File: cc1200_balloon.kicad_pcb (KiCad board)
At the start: 4 copper layers, 50 x 30 mm, 117 parts, among them J101 BATT pads, J201 LoRa ANT pads, J202 SWD+DBG pads, J301 434MHz ANT pads, J401 GNSS ANT, J501 BMV080, Q101 DMG3401LSN-7, Q102 DMG3401LSN-7, SW101 PWR, U201 Wio-E5, U301 CC1200, U401 AT6558R-5N32, U501 SCD40-D-R2, U502 AS3935-BQFT, U503 BME688, U504 BME688, X301 40MHz, X401 TCXO 26MHz, X402 32.768kHz

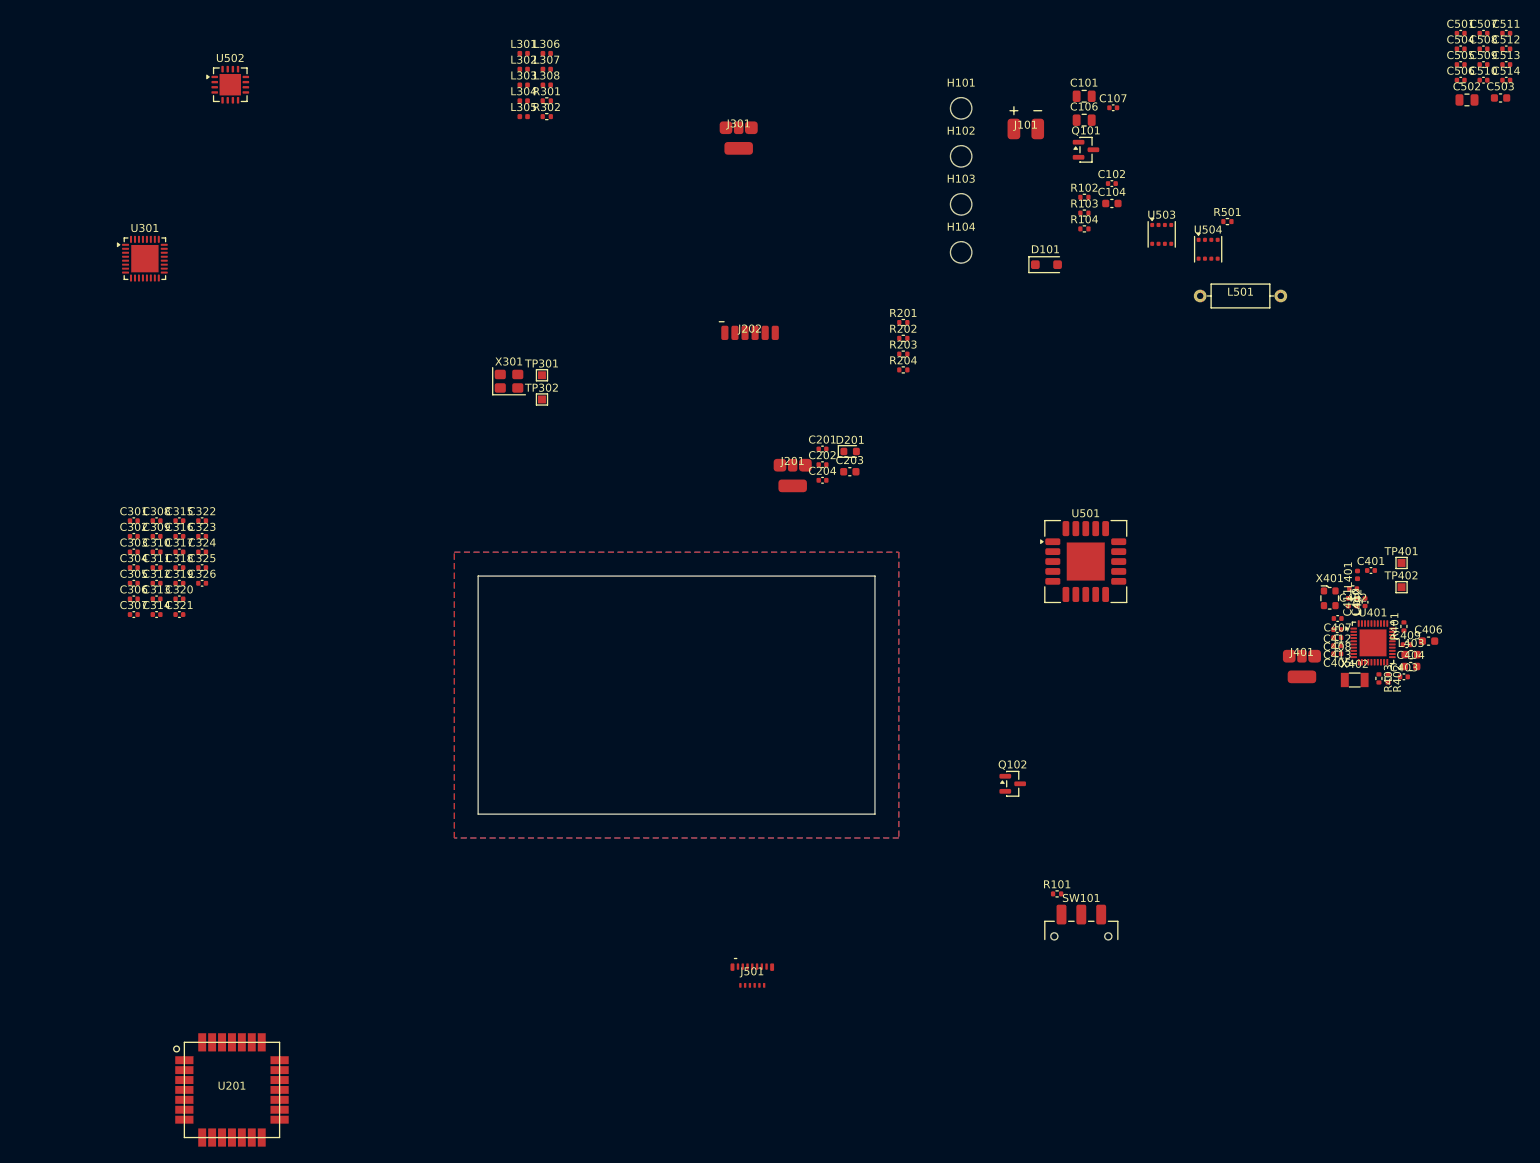
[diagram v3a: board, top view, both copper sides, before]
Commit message: Clean up schematic. Add component groups to PCB.
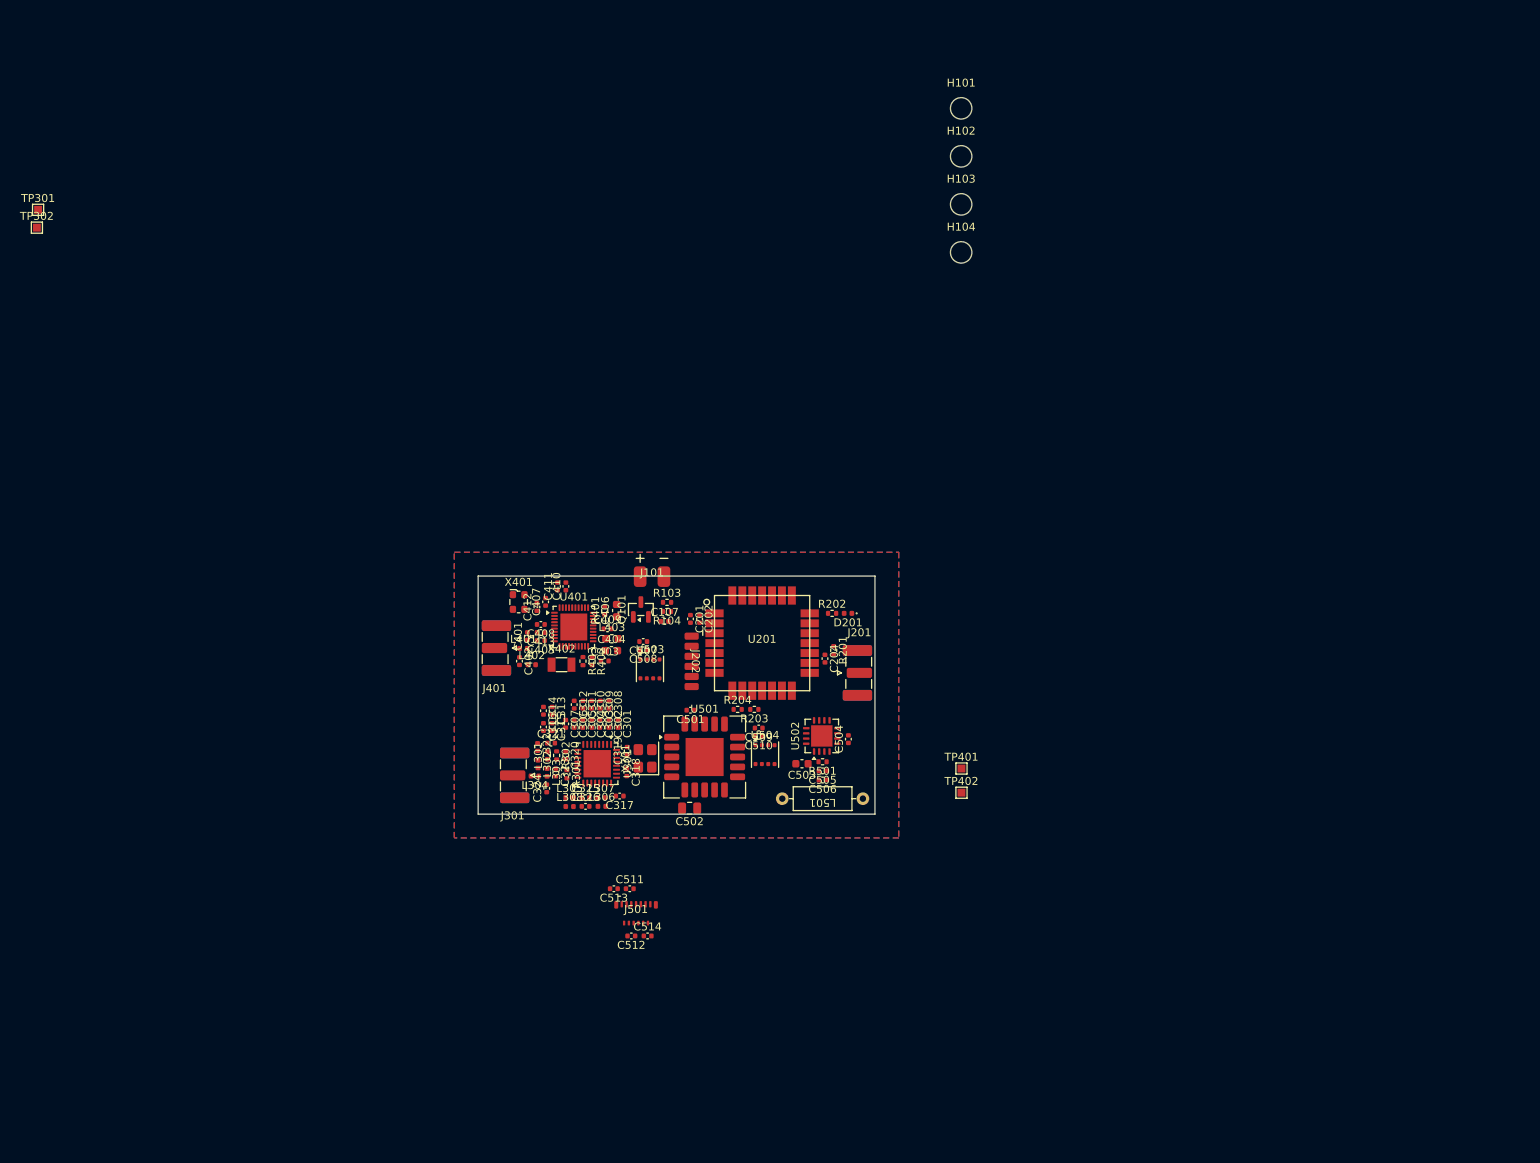
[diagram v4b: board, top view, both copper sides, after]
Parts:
- removed C101, C106: 22u, Capacitor_SMD:C_0805_2012Metric
- removed C102: 1u, Capacitor_SMD:C_0402_1005Metric
- removed C104, C203: 10u, Capacitor_SMD:C_0603_1608Metric
- removed D101: SMF6.5A, Diode_SMD:D_SOD-123F
- removed Q102: DMG3401LSN-7, Package_TO_SOT_SMD:SOT-23
- removed R101: 100k, Resistor_SMD:R_0402_1005Metric
- removed R102: 10k, Resistor_SMD:R_0402_1005Metric
- removed SW101: PWR, Button_Switch_SMD:SW_SPDT_CK_JS102011SAQN
- C202: value 1u -> 4.7u
- D201: footprint LED_SMD:LED_0603_1608Metric -> LED_SMD:LED_0402_1005Metric
- J201, J301, J401: footprint cc1200_balloon:SolderPad_Coax_Pigtail -> Connector_Coaxial:SMA_Samtec_SMA-J-P-H-ST-EM1_EdgeMount
- moved C512 157.0 mm to (94.3, 130.3), turned to 180 degrees
- moved C511 154.3 mm to (94.1, 124.4)
- moved C513 153.1 mm to (92.1, 124.4), turned to 180 degrees
- moved C514 152.8 mm to (96.3, 130.3)
- moved C502 132.5 mm to (101.7, 114.2), turned to 180 degrees
- moved C507 130.7 mm to (95.8, 93.2), turned to 180 degrees
- moved C508 130.2 mm to (95.8, 94.3), turned to 180 degrees
- moved C501 129.2 mm to (101.8, 101.9), turned to 180 degrees
- moved C509 123.8 mm to (110.3, 104.2), turned to 180 degrees
- moved C510 123.2 mm to (110.3, 105.2), turned to 180 degrees
- moved C503 121.6 mm to (115.8, 108.7), turned to 180 degrees
- moved C505 119.9 mm to (118.4, 109.5), turned to 180 degrees
- moved C506 119.3 mm to (118.4, 110.7), turned to 180 degrees
- moved C504 116.3 mm to (121.7, 105.5), turned to 90 degrees
- moved U502 110.9 mm to (118.3, 105.2), turned to 90 degrees
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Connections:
- net /Power/VBAT_IN renamed /MCU/VBATT_IN
- net VBAT_SENSE renamed /MCU/BATT_VSENSE
- C317 pad 1: Net-(U301-LPF0) -> Net-(U301-LPF1)
- C317 pad 2: Net-(U301-LPF1) -> Net-(U301-LPF0)
- C321 pad 1: /CC1200 Radio/RF_PA -> /CC1200 Radio/RF_TX1
- C321 pad 2: /CC1200 Radio/RF_TX1 -> /CC1200 Radio/RF_PA
- C325 pad 1: /CC1200 Radio/RF_LNAP -> /CC1200 Radio/RF_RX1
- C325 pad 2: /CC1200 Radio/RF_RX1 -> /CC1200 Radio/RF_LNAP
- C505 pad 1: Net-(C505-Pad1) -> /Sensors/AS_ANT_P
- L501 pad 1: Net-(C505-Pad1) -> /Sensors/AS_ANT_P
- Q101 pad 2: VBATT -> +BATT
- R501 pad 1: Net-(C505-Pad1) -> /Sensors/AS_ANT_P
- U501 pad 10: SDA -> SCL
- U501 pad 9: SCL -> SDA
- U502 pad 11: SCL -> SDA
- U502 pad 13: SDA -> SCL
- U503 pad 3: SDA -> SCL
- U503 pad 4: SCL -> SDA
- U504 pad 3: SDA -> SCL
- U504 pad 4: SCL -> SDA

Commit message: Inital routing
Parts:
- removed C502: 22u, Capacitor_SMD:C_0805_2012Metric
- removed C512, C513: 1u, Capacitor_SMD:C_0402_1005Metric
- removed C514: 100n, Capacitor_SMD:C_0402_1005Metric
- J101, J202: moved to B.Cu
- moved TP302 62.3 mm to (66.8, 81.5)
- moved TP301 62.2 mm to (66.8, 79.2)
- moved R104 48.7 mm to (50.1, 89.5)
- moved C107 48.7 mm to (49.8, 90.8)
- moved Q101 48.7 mm to (46.8, 89.3)
- moved R103 48.7 mm to (50.1, 88.4)
- moved J101 47.5 mm to (49.5, 87.7), turned to 180 degrees
- moved L501 33.5 mm to (97.1, 87.2), turned to 0 degrees
- moved C506 30.0 mm to (97.1, 89.5), turned to 0 degrees
- moved C504 29.5 mm to (94.1, 95.0), turned to -90 degrees
- moved C505 28.4 mm to (97.1, 90.7), turned to 0 degrees
- moved R501 27.0 mm to (97.1, 91.8), turned to 0 degrees
- moved C503 24.5 mm to (99.0, 90.8), turned to 90 degrees
- moved U502 23.4 mm to (97.2, 95.1), turned to -90 degrees
- moved C501 22.0 mm to (80.0, 99.1)
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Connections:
- U501 pad 10: SCL -> SDA
- U501 pad 9: SDA -> SCL
- U502 pad 11: SDA -> SCL
- U502 pad 13: SCL -> SDA
- U503 pad 3: SCL -> SDA
- U503 pad 4: SDA -> SCL
- U504 pad 3: SCL -> SDA
- U504 pad 4: SDA -> SCL
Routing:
- net +BATT: track 0.00 -> 21.0 mm, vias 0 -> 1
- net SPI_MISO: track 0.00 -> 18.1 mm, vias 0 -> 1
- net /CC1200 Radio/XOSC_Q1: track 0.00 -> 8.01 mm
- net /CC1200 Radio/RF_LNAN: track 0.00 -> 5.81 mm
- net /CC1200 Radio/RF_TX2: track 0.00 -> 4.57 mm
- net /CC1200 Radio/RF_PA: track 0.00 -> 4.37 mm
- net /CC1200 Radio/RF_TRXSW: track 0.00 -> 4.16 mm
- net /CC1200 Radio/RF_LNAP: track 0.00 -> 3.93 mm
- net /CC1200 Radio/XOSC_Q2: track 0.00 -> 3.80 mm
- net /CC1200 Radio/RF_RX1: track 0.00 -> 3.70 mm
- net SPI_MOSI: track 0.00 -> 3.55 mm, vias 0 -> 1
- net /CC1200 Radio/CC_RBIAS: track 0.00 -> 3.42 mm
- net Net-(U301-LPF1): track 0.00 -> 3.13 mm
- net Net-(U301-LPF0): track 0.00 -> 3.03 mm
- net RADIO_CS: track 0.00 -> 2.28 mm, vias 0 -> 1
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
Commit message: More routing.
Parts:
- TP301, TP302, TP401, TP402: moved to B.Cu
- moved R103 90.5 mm to (138.4, 108.4)
- moved C107 90.5 mm to (138.1, 110.8)
- moved J101 90.5 mm to (137.8, 107.7)
- moved Q101 90.5 mm to (135.1, 109.3)
- moved R104 90.5 mm to (138.4, 109.6)
- moved TP401 52.1 mm to (86.0, 95.3), turned to 180 degrees
- moved TP402 50.8 mm to (88.0, 95.3), turned to 180 degrees
- moved TP302 29.6 mm to (91.2, 98.2), turned to -90 degrees
- moved TP301 29.4 mm to (89.2, 98.2), turned to -90 degrees
- moved J202 12.4 mm to (113.0, 87.5), turned to 0 degrees
- moved C503 2.98 mm to (100.9, 93.0), turned to 0 degrees
- moved R501 2.94 mm to (100.0, 91.3), turned to 90 degrees
- moved D201 2.55 mm to (121.4, 88.9), turned to 0 degrees
- moved C506 1.90 mm to (97.7, 91.3), turned to 90 degrees
- moved C505 1.87 mm to (98.8, 91.3), turned to 90 degrees
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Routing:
- net SDA: track 2.08 -> 43.9 mm, vias 0 -> 4
- net SCL: track 0.00 -> 41.2 mm, vias 0 -> 4
- net GNSS_PPS: track 0.00 -> 27.6 mm
- net RADIO_RST: track 0.00 -> 15.8 mm, vias 0 -> 2
- net NRST: track 0.00 -> 15.6 mm, vias 0 -> 1
- net SPI_MISO: track 18.1 -> 3.87 mm, vias 1 -> 3
- net /MCU/DBG_TX: track 0.00 -> 13.1 mm, vias 0 -> 1
- net +BATT: track 21.0 -> 33.3 mm, vias 1 -> 16
- net /MCU/SWCLK: track 0.00 -> 9.96 mm, vias 0 -> 1
- net /MCU/SWDIO: track 0.00 -> 8.41 mm, vias 0 -> 1
- net /GNSS/GNSS_VX: track 0.00 -> 5.48 mm
- net /GNSS/GNSS_ANT_BIAS: track 0.00 -> 4.16 mm
- net /GNSS/GNSS_VCORE: track 1.75 -> 5.30 mm
- net /GNSS/GNSS_XREF: track 0.00 -> 3.03 mm
- net /GNSS/GNSS_RTC_O: track 0.00 -> 2.43 mm
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
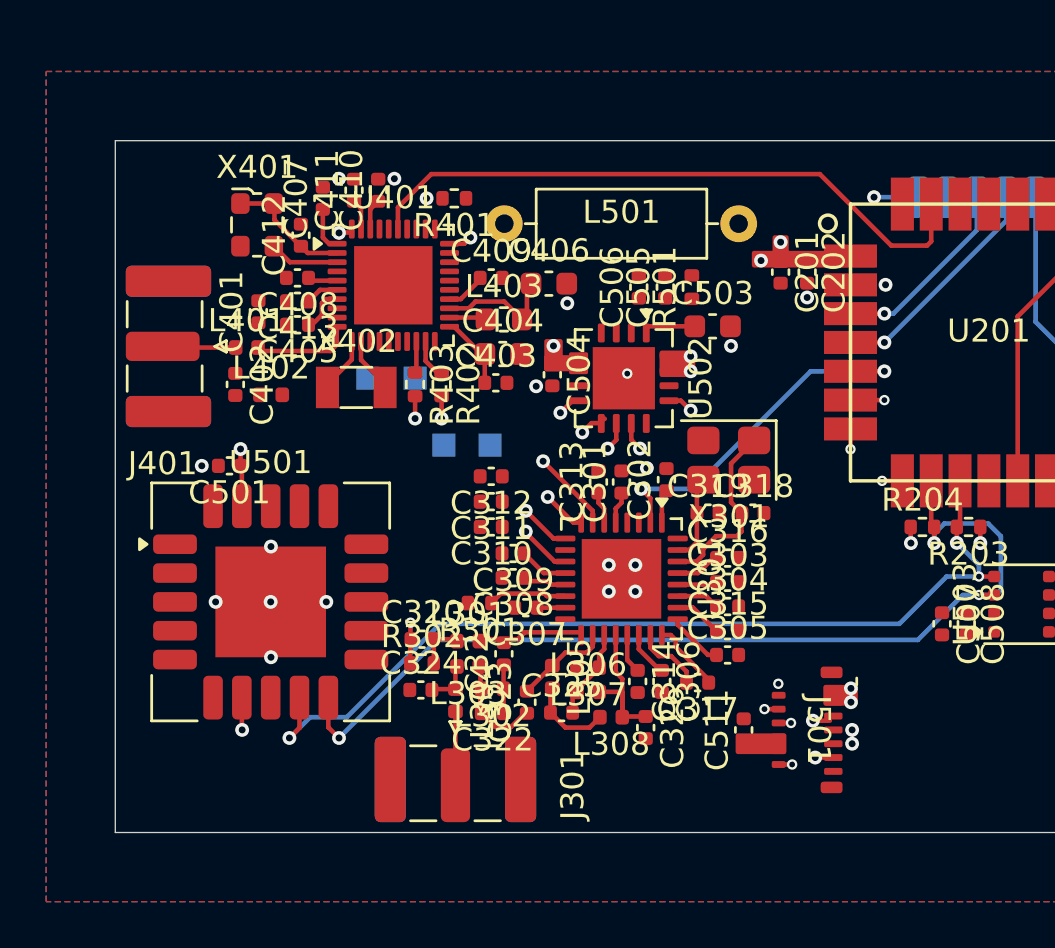
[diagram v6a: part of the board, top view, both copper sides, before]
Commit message: Clean up schematic. Add component groups to PCB.
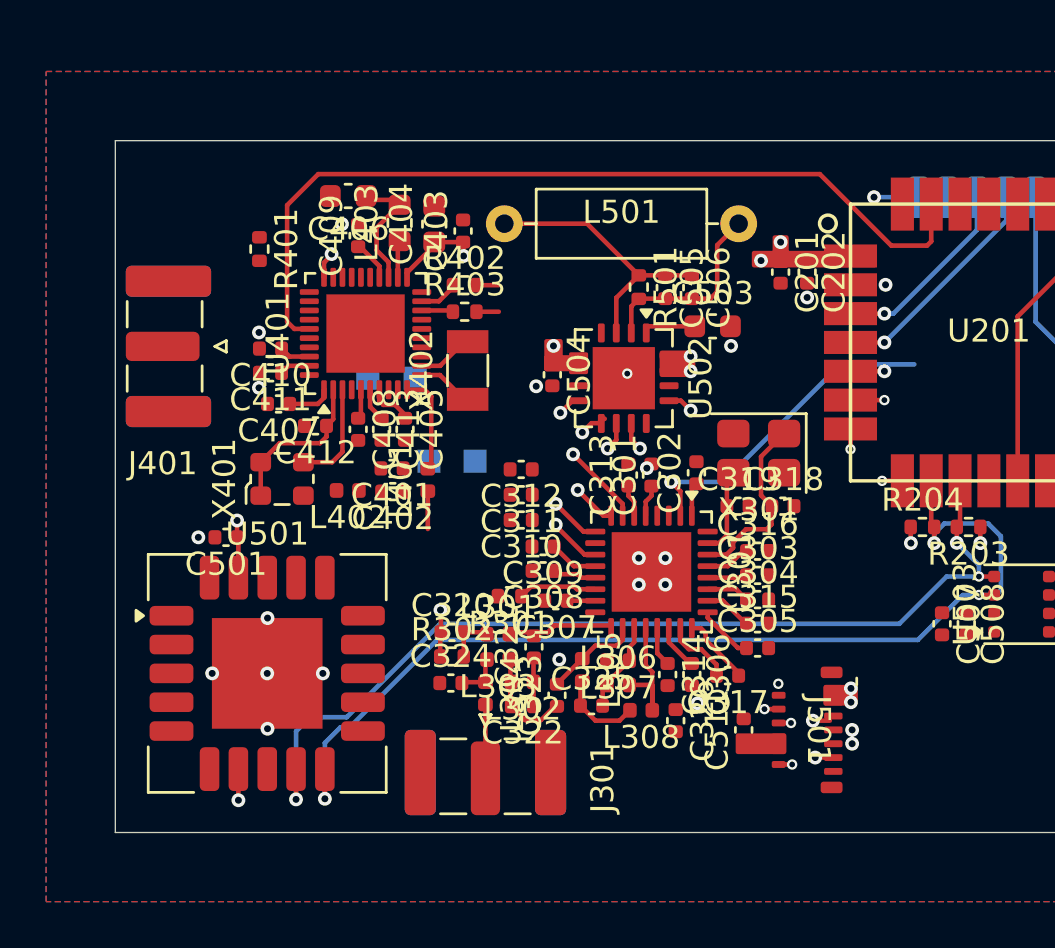
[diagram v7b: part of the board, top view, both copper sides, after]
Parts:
- moved X401 11.1 mm to (82.2, 99.7), turned to 90 degrees
- moved L401 9.72 mm to (88.5, 99.7), turned to 90 degrees
- moved C406 9.49 mm to (85.1, 87.4), turned to 180 degrees
- moved C407 9.12 mm to (82.1, 96.4), turned to 180 degrees
- moved C401 8.93 mm to (87.0, 99.2), turned to 180 degrees
- moved R401 8.73 mm to (81.2, 89.7), turned to -90 degrees
- moved C411 8.71 mm to (81.7, 95.1), turned to 180 degrees
- moved C410 8.30 mm to (81.7, 94.0), turned to 180 degrees
- moved C412 8.29 mm to (83.7, 97.4), turned to 180 degrees
- moved C402 8.26 mm to (87.0, 100.2), turned to 180 degrees
- moved C408 7.07 mm to (85.5, 97.5), turned to -90 degrees
- moved C403 6.73 mm to (90.1, 88.9), turned to 90 degrees
- moved C413 6.64 mm to (86.5, 97.5), turned to -90 degrees
- moved C405 6.50 mm to (87.6, 97.5), turned to -90 degrees
- moved C404 6.37 mm to (88.8, 88.6), turned to 90 degrees
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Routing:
- net /Sensors/AS_ANT_P: track 0.00 -> 12.0 mm
- net GNSS_PPS: track 27.6 -> 37.6 mm
- net /Sensors/AS_ANT_N: track 0.00 -> 8.76 mm
- net SDA: track 43.9 -> 46.4 mm
- net SCL: track 41.2 -> 43.1 mm
- net /GNSS/GNSS_XREF: track 3.03 -> 4.58 mm
- net /GNSS/GNSS_VX: track 5.48 -> 6.92 mm
- net /CC1200 Radio/RF_LNAN: track 6.84 -> 5.81 mm
- net /GNSS/GNSS_RF_IN: track 0.56 -> 0.00 mm, vias 1 -> 0
- net +BATT: track 33.3 -> 33.6 mm, vias 16 -> 17
- net GNSS_TX: vias 1 -> 0
- net GNSS_RX: vias 1 -> 0
- net GND: vias 25 -> 26

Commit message: Route, mostly done.
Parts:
- added JP1: IAB0, cc1200_balloon:Jumper_3_0402, F.Cu at (108.8, 106.7)
- added JP2: IAB1, cc1200_balloon:Jumper_3_0402, F.Cu at (108.8, 107.7)
- moved J101 60.9 mm to (80.0, 88.2)
- moved Q101 58.7 mm to (80.0, 89.3), turned to 0 degrees
- moved H102 39.6 mm to (133.8, 71.7)
- moved H103 39.6 mm to (133.8, 77.7)
- moved H101 39.6 mm to (133.8, 65.6)
- moved H104 39.6 mm to (133.8, 83.8)
- moved C107 29.7 mm to (120.2, 87.0), turned to -90 degrees
- moved R104 28.4 mm to (121.8, 86.5), turned to 0 degrees
- moved R103 26.6 mm to (121.8, 87.6), turned to 180 degrees
- moved TP401 20.7 mm to (66.3, 88.8)
- moved TP402 20.7 mm to (68.3, 88.8)
- moved TP301 17.0 mm to (71.6, 100.0)
- moved TP302 17.0 mm to (73.6, 100.0)
- moved C402 9.17 mm to (79.9, 94.5), turned to 90 degrees
- moved L401 8.96 mm to (80.4, 96.0), turned to 0 degrees
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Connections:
- J501 pad 11: SPI_MISO -> /Sensors/IAB1
- J501 pad 4: PM_CS -> /Sensors/IAB0
- J501 pad 5: SPI_MOSI -> SDA
- J501 pad 6: SPI_SCK -> SCL
- J501 pad 7: GND -> +BATT
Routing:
- net GNSS_ONOFF: track 1.14 -> 53.3 mm, vias 1 -> 2
- net GNSS_RX: track 0.82 -> 35.4 mm, vias 0 -> 2
- net PM_IRQ: track 0.58 -> 33.9 mm, vias 1 -> 2
- net GNSS_TX: track 0.82 -> 33.4 mm, vias 0 -> 2
- net LIGHTNING_IRQ: track 1.24 -> 32.4 mm, vias 1 -> 2
- net SPI_MOSI: track 4.29 -> 34.0 mm
- net SCL: track 43.1 -> 71.2 mm, vias 4 -> 5
- net +BATT: track 33.6 -> 59.1 mm, vias 17 -> 41
- net RADIO_IRQ: track 0.00 -> 25.4 mm, vias 0 -> 2
- net RADIO_CS: track 2.28 -> 27.5 mm, vias 1 -> 2
- net SDA: track 46.4 -> 66.6 mm, vias 4 -> 5
- net SPI_SCK: track 3.33 -> 23.0 mm, vias 3 -> 2
- net /Sensors/IAB0: track 0.00 -> 17.2 mm, vias 0 -> 2
- net /GNSS/GNSS_ANT_BIAS: track 4.31 -> 18.6 mm
- net SPI_MISO: track 3.87 -> 16.5 mm, vias 3 -> 2
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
